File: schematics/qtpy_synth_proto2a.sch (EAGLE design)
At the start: 25 parts, among them IC1 H11L1MS, J1 AUDIO-JACK-TRRS, J2 AUDIO-JACK-TRRS, P1 10k, P2 10k, U1 ADAFRUIT_QTPYM0

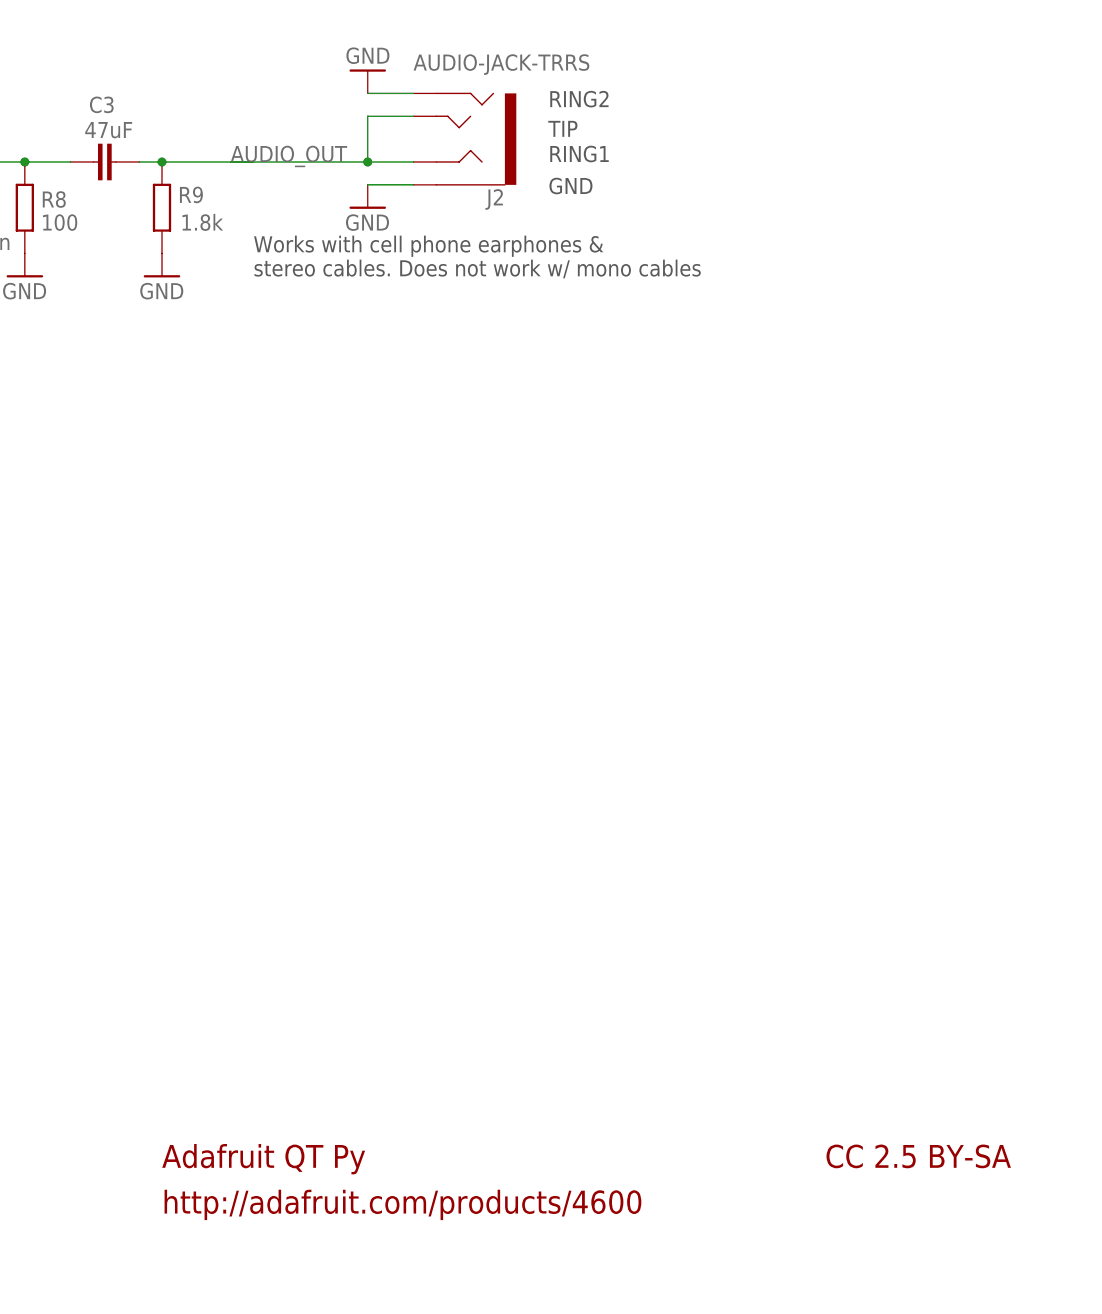
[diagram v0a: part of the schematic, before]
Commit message: fix name, add hwtest
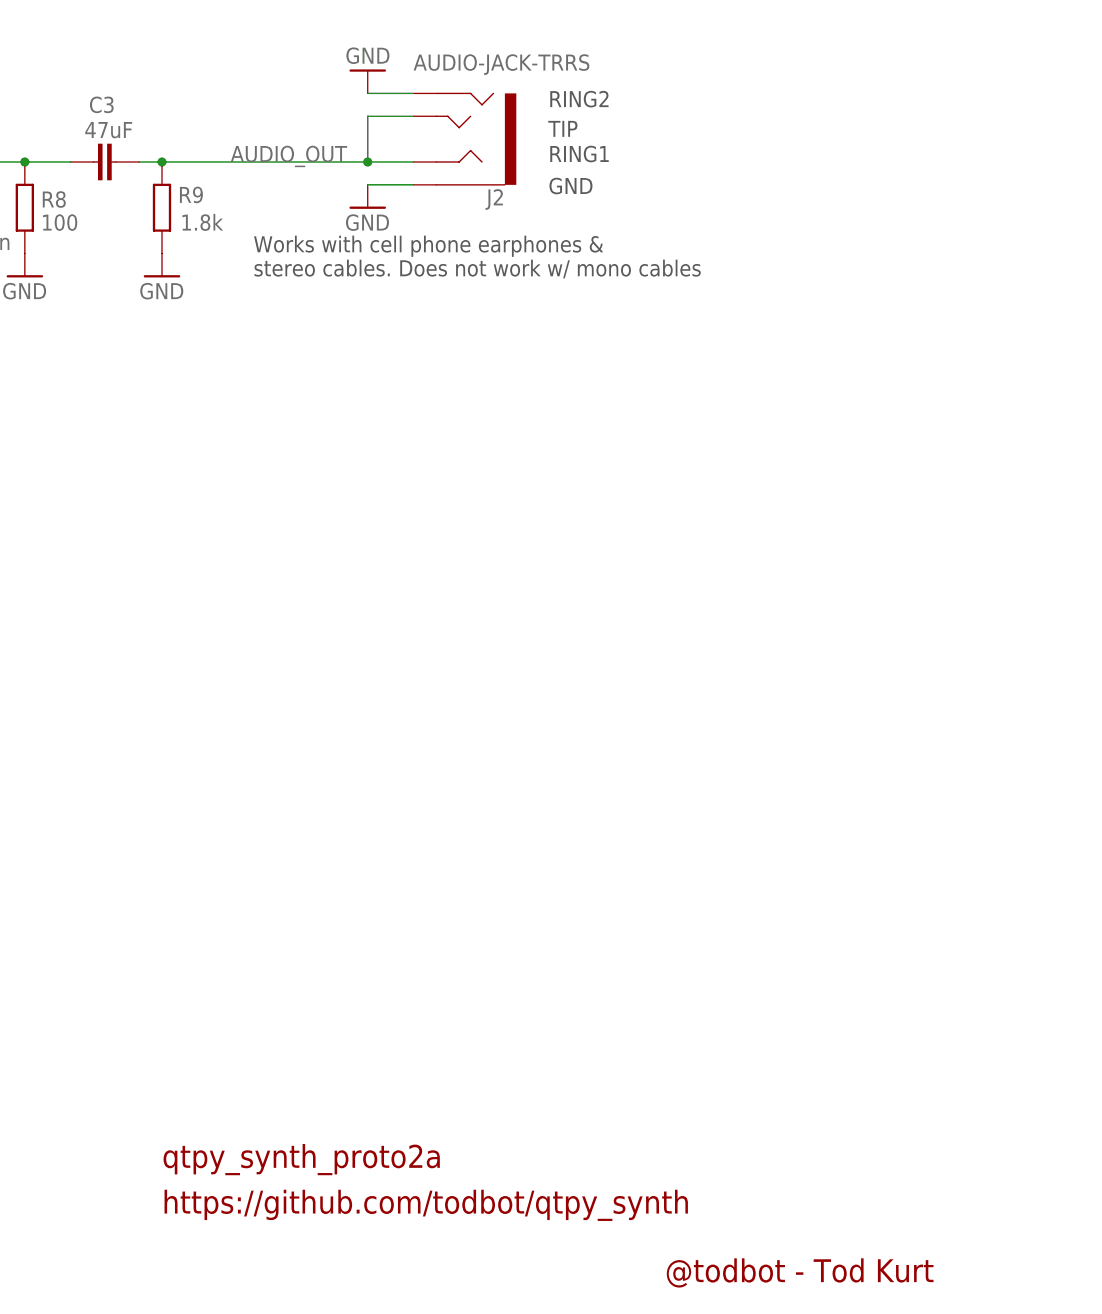
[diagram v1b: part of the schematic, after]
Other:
- note added: "@todbot - Tod Kurt"
- note added: "https://github.com/todbot/qtpy_synth"
- note added: "qtpy_synth_proto2a"
- note removed: "Adafruit QT Py"
- note removed: "CC 2.5 BY-SA"
- note removed: "http://adafruit.com/products/4600"
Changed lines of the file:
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@@
 <sheet>
 <plain>
-<text x="175.26" y="30.48" size="2.54" layer="94">Adafruit QT Py</text>
-<text x="175.26" y="25.4" size="2.54" layer="94">http://adafruit.com/products/4600</text>
-<text x="248.92" y="30.48" size="2.54" layer="94">CC 2.5 BY-SA</text>
+<text x="175.26" y="30.48" size="2.54" layer="94">qtpy_synth_proto2a</text>
+<text x="175.26" y="25.4" size="2.54" layer="94">https://github.com/todbot/qtpy_synth</text>
 <text x="218.186" y="171.704" size="1.778" layer="97" rot="MR180">RING2</text>
 <text x="218.186" y="177.8" size="1.778" layer="97" rot="MR180">RING1</text>
@@
 <text x="185.42" y="129.54" size="1.778" layer="97">Works with cell phone earphones &amp;
 stereo cables. Does not work w/ mono cables</text>
+<text x="231.14" y="17.78" size="2.54" layer="94">@todbot - Tod Kurt</text>
 </plain>
 <instances>
@@
 <net name="AUDIO_OUT" class="0">
 <segment>
-<pinref part="R9" gate="G$1" pin="1"/>
-<pinref part="C3" gate="G$1" pin="2"/>
-<wire x1="185.42" y1="142.24" x2="175.26" y2="142.24" width="0.1524" layer="91"/>
-<wire x1="172.72" y1="142.24" x2="175.26" y2="142.24" width="0.1524" layer="91"/>
-<junction x="175.26" y="142.24"/>
-</segment>
-<segment>
 <pinref part="J2" gate="G$1" pin="RING1"/>
 <wire x1="203.2" y1="142.24" x2="198.12" y2="142.24" width="0.1524" layer="91"/>
 <wire x1="198.12" y1="142.24" x2="198.12" y2="147.32" width="0.1524" layer="91"/>
-<junction x="198.12" y="142.24"/>
 <label x="182.88" y="142.24" size="1.778" layer="95"/>
 <pinref part="J2" gate="G$1" pin="TIP"/>
 <wire x1="203.2" y1="147.32" x2="198.12" y2="147.32" width="0.1524" layer="91"/>
-<wire x1="198.12" y1="142.24" x2="182.88" y2="142.24" width="0.1524" layer="91"/>
-</segment>
-</net>
+<pinref part="R9" gate="G$1" pin="1"/>
+<pinref part="C3" gate="G$1" pin="2"/>
+<wire x1="172.72" y1="142.24" x2="175.26" y2="142.24" width="0.1524" layer="91"/>
+<wire x1="198.12" y1="142.24" x2="175.26" y2="142.24" width="0.1524" layer="91"/>
+<junction x="198.12" y="142.24"/>
+<junction x="175.26" y="142.24"/>
+</segment>
+</net>
